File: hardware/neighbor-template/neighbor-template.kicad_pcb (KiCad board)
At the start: 4 copper layers, 70.6 x 53.3 mm, 7 parts, among them J1 NEIGHBOR1, J2 NEIGHBOR2, J7 BONUS_ROW

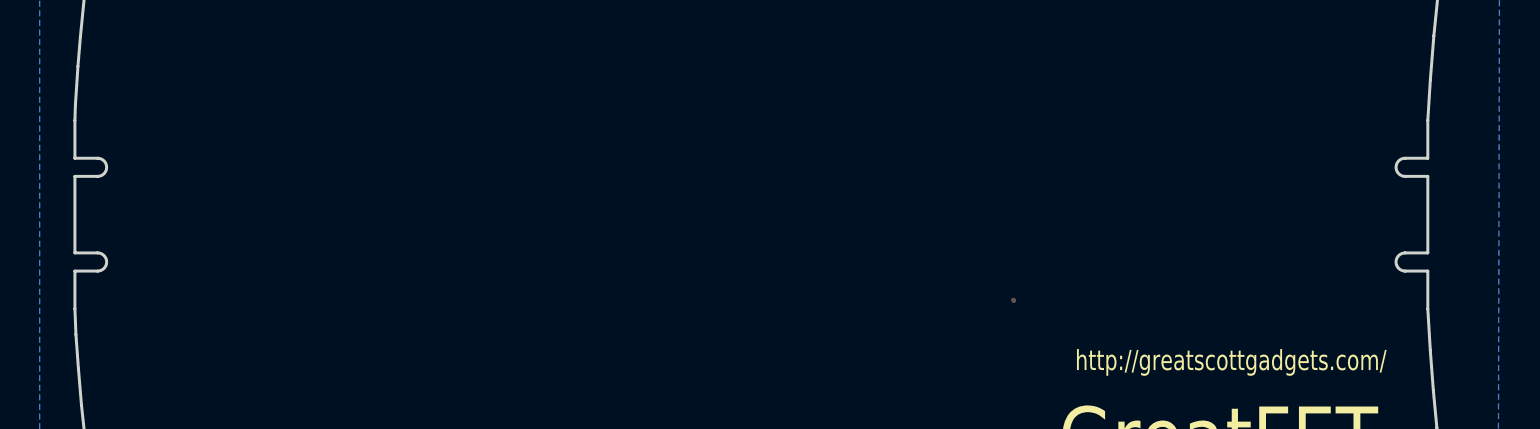
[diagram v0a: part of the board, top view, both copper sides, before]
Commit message: neighbor template: removed USB connector edge cutouts
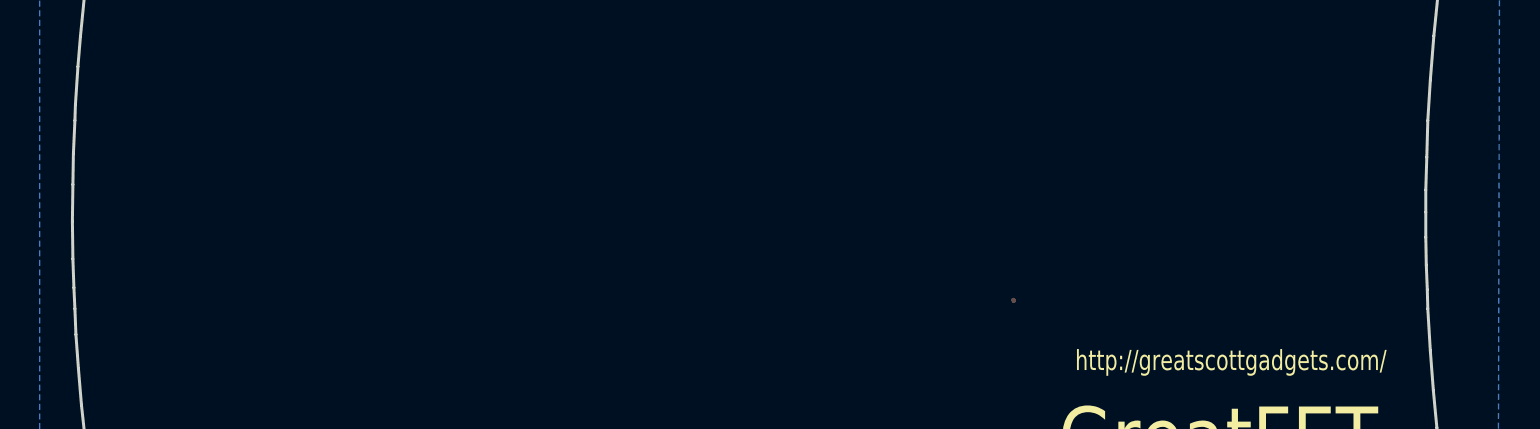
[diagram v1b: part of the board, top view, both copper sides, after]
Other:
- board size 70.6 x 53.3 mm -> 70.7 x 53.3 mm
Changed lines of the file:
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@@
     (links 41)
     (no_connects 0)
-    (area 105.842999 71.044999 176.605001 124.535001)
+    (area 105.715999 71.044999 176.605001 124.535001)
     (thickness 1.6)
-    (drawings 127)
+    (drawings 122)
     (tracks 4)
     (zones 0)
@@
       (net 1 GND))
   )
+  (gr_line (start 105.8672 101.473) (end 105.918 102.5398) (angle 90) (layer Edge.Cuts) (width 0.15))
+  (gr_line (start 105.8164 100.0252) (end 105.8672 101.473) (angle 90) (layer Edge.Cuts) (width 0.15))
+  (gr_line (start 105.791 98.1202) (end 105.8164 100.0252) (angle 90) (layer Edge.Cuts) (width 0.15))
+  (gr_line (start 105.8164 96.266) (end 105.791 98.1202) (angle 90) (layer Edge.Cuts) (width 0.15))
+  (gr_line (start 105.8418 94.7166) (end 105.8164 96.266) (angle 90) (layer Edge.Cuts) (width 0.15))
+  (gr_line (start 105.918 93.0402) (end 105.8418 94.7166) (angle 90) (layer Edge.Cuts) (width 0.15))
+  (gr_line (start 174.117 101.5746) (end 174.1424 102.5398) (angle 90) (layer Edge.Cuts) (width 0.15))
+  (gr_line (start 174.0662 100.33) (end 174.117 101.5746) (angle 90) (layer Edge.Cuts) (width 0.15))
+  (gr_line (start 174.0408 98.933) (end 174.0662 100.33) (angle 90) (layer Edge.Cuts) (width 0.15))
+  (gr_line (start 174.0408 97.663) (end 174.0408 98.933) (angle 90) (layer Edge.Cuts) (width 0.15))
+  (gr_line (start 174.0408 96.5454) (end 174.0408 97.663) (angle 90) (layer Edge.Cuts) (width 0.15))
+  (gr_line (start 174.0916 94.8944) (end 174.0408 96.5454) (angle 90) (layer Edge.Cuts) (width 0.15))
+  (gr_line (start 174.1424 93.0402) (end 174.0916 94.8944) (angle 90) (layer Edge.Cuts) (width 0.15))
   (gr_text "24 September 2015" (at 149.6314 116.9416) (layer F.SilkS)
     (effects (font (size 1.016 0.762) (thickness 0.1524)))
@@
   (gr_line (start 174.2694 91.0082) (end 174.4472 88.773) (angle 90) (layer Edge.Cuts) (width 0.15))
   (gr_line (start 174.1424 93.0402) (end 174.2694 91.0082) (angle 90) (layer Edge.Cuts) (width 0.15))
-  (gr_line (start 105.918 100.6348) (end 105.918 102.5398) (angle 90) (layer Edge.Cuts) (width 0.15))
-  (gr_line (start 107.061 100.6348) (end 105.918 100.6348) (angle 90) (layer Edge.Cuts) (width 0.15))
-  (gr_line (start 105.918 99.7204) (end 107.061 99.7204) (angle 90) (layer Edge.Cuts) (width 0.15))
-  (gr_line (start 105.918 95.8596) (end 105.918 99.7204) (angle 90) (layer Edge.Cuts) (width 0.15))
-  (gr_line (start 107.061 95.8596) (end 105.918 95.8596) (angle 90) (layer Edge.Cuts) (width 0.15))
-  (gr_line (start 105.918 94.9452) (end 105.918 93.0402) (angle 90) (layer Edge.Cuts) (width 0.15))
-  (gr_line (start 107.061 94.9452) (end 105.918 94.9452) (angle 90) (layer Edge.Cuts) (width 0.15))
-  (gr_arc (start 107.061 100.1776) (end 107.061 99.7204) (angle 180) (layer Edge.Cuts) (width 0.15))
-  (gr_arc (start 107.061 95.4024) (end 107.061 94.9452) (angle 180) (layer Edge.Cuts) (width 0.15))
-  (gr_line (start 174.1424 100.6348) (end 174.1424 102.5398) (angle 90) (layer Edge.Cuts) (width 0.15))
-  (gr_line (start 172.9994 100.6348) (end 174.1424 100.6348) (angle 90) (layer Edge.Cuts) (width 0.15))
-  (gr_line (start 174.1424 99.7204) (end 172.9994 99.7204) (angle 90) (layer Edge.Cuts) (width 0.15))
-  (gr_line (start 174.1424 95.8596) (end 174.1424 99.7204) (angle 90) (layer Edge.Cuts) (width 0.15))
-  (gr_line (start 172.9994 95.8596) (end 174.1424 95.8596) (angle 90) (layer Edge.Cuts) (width 0.15))
-  (gr_line (start 174.1424 94.9452) (end 174.1424 93.0402) (angle 90) (layer Edge.Cuts) (width 0.15))
-  (gr_line (start 172.9994 94.9452) (end 174.1424 94.9452) (angle 90) (layer Edge.Cuts) (width 0.15))
-  (gr_arc (start 172.9994 100.1776) (end 172.9994 100.6348) (angle 180) (layer Edge.Cuts) (width 0.15))
-  (gr_arc (start 172.9994 95.4024) (end 172.9994 95.8596) (angle 180) (layer Edge.Cuts) (width 0.15))
   (gr_arc (start 112.3188 74.93) (end 112.3188 71.12) (angle -70) (layer Cmts.User) (width 0.15))
   (gr_arc (start 172.72 120.65) (end 176.53 120.65) (angle 90) (layer Edge.Cuts) (width 0.15))

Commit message: neighbor-template: track cleanup
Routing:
- removed copper zone on B.Cu, net /VBUS
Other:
- board text added: "27 September 2015"
- board text removed: "24 September 2015"
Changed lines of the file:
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@@
     (links 41)
     (no_connects 0)
-    (area 105.715999 71.044999 176.605001 124.535001)
+    (area 104.14 68.58 275.715801 199.465001)
     (thickness 1.6)
     (drawings 122)
-    (tracks 4)
+    (tracks 0)
     (zones 0)
     (modules 7)
@@
   (gr_line (start 174.0916 94.8944) (end 174.0408 96.5454) (angle 90) (layer Edge.Cuts) (width 0.15))
   (gr_line (start 174.1424 93.0402) (end 174.0916 94.8944) (angle 90) (layer Edge.Cuts) (width 0.15))
-  (gr_text "24 September 2015" (at 149.6314 116.9416) (layer F.SilkS)
+  (gr_text "27 September 2015" (at 149.6314 116.9416) (layer F.SilkS)
     (effects (font (size 1.016 0.762) (thickness 0.1524)))
   )
@@
   (gr_line (start 172.72 124.46) (end 112.3188 124.46) (angle 90) (layer Edge.Cuts) (width 0.15))
   (gr_line (start 112.3188 71.12) (end 172.72 71.12) (angle 90) (layer Edge.Cuts) (width 0.15))
-  (segment (start 153.24074 102.08768) (end 153.2636 102.11054) (width 0.2032) (layer F.Cu) (net 0))
-  (segment (start 153.2636 102.11054) (end 153.2636 102.1334) (width 0.2032) (layer F.Cu) (net 0))
-  (segment (start 153.2636 102.1334) (end 153.24074 102.08768) (width 0.2032) (layer F.Cu) (net 0))
-  (segment (start 161.29 78.8416) (end 161.29 78.74) (width 0.2032) (layer F.Cu) (net 0) (status 30))
   (zone (net 2) (net_name VCC) (layer C3.Cu) (hatch edge 0.508)
     (connect_pads (clearance 0.254))
@@
       )
     )
-  )
-  (zone (net 3) (net_name /VBUS) (layer B.Cu) (hatch edge 0.508)
-    (connect_pads (clearance 0.254))
-    (min_thickness 0.254)
-    (fill yes (arc_segments 16) (thermal_gap 0.254) (thermal_bridge_width 0.508))
-    (polygon
-      (pts
-        (xy 104.14 68.58) (xy 177.8 68.58) (xy 177.6984 111.5822) (xy 172.4406 112.3696) (xy 173.3042 117.3226)
-        (xy 177.8 116.6114) (xy 177.8 127) (xy 104.14 127)
-      )
-    )
